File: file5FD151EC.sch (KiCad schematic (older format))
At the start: 5 parts, among them J3 Conn_ARM_JTAG_SWD_10

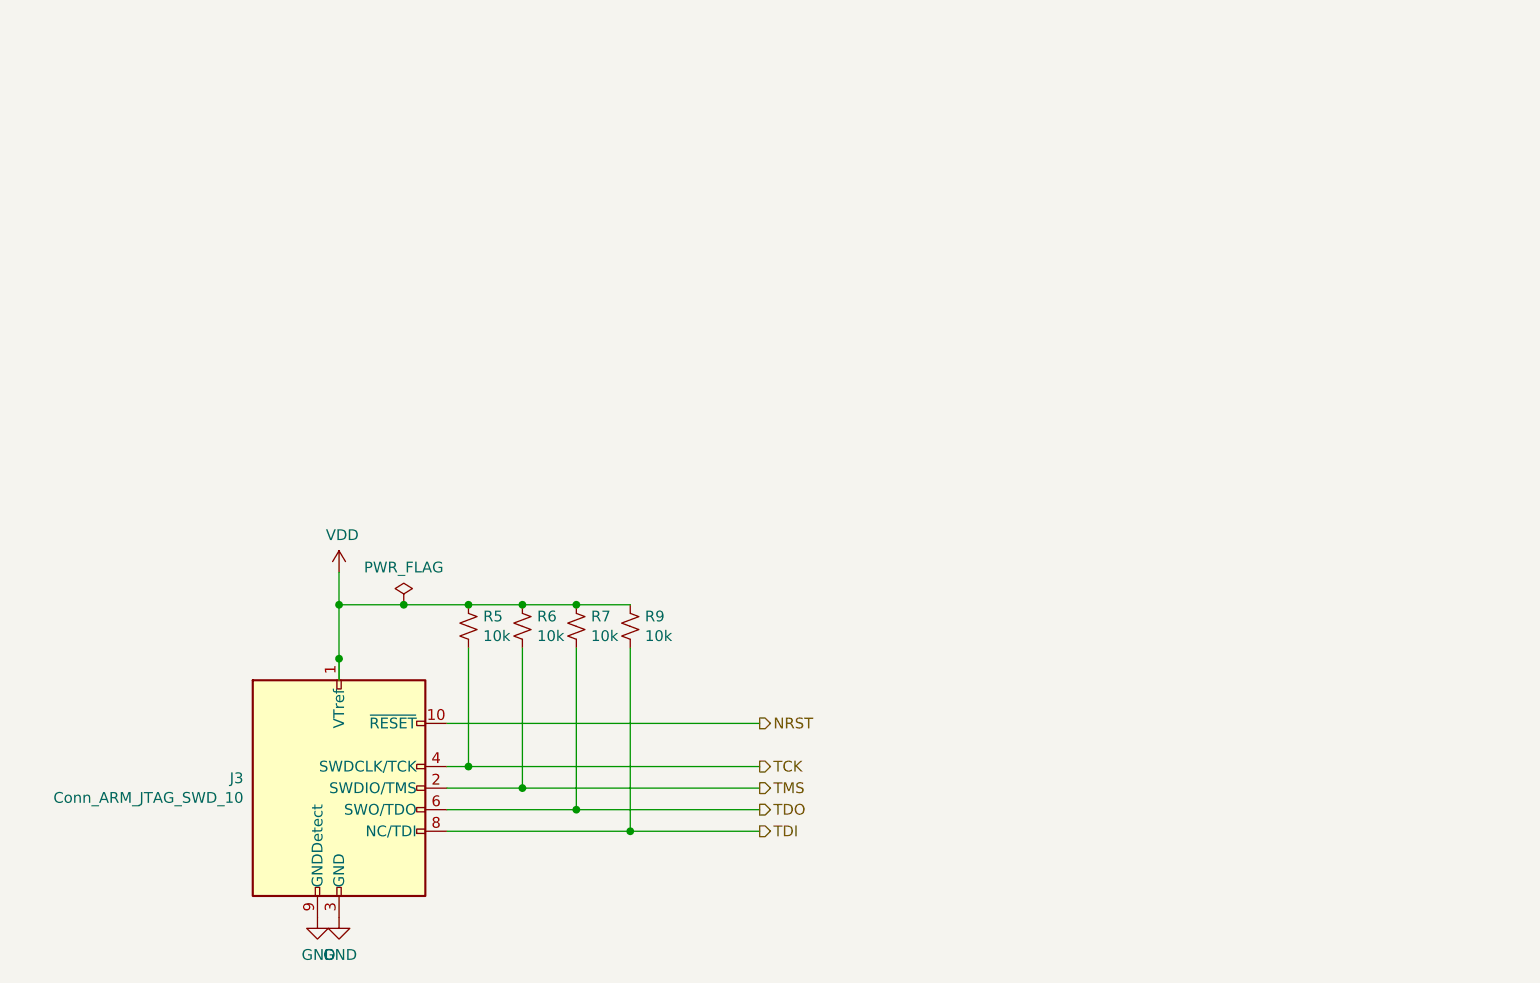
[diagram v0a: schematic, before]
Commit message: Change PS to SMPS 5v, LDO 3.3V
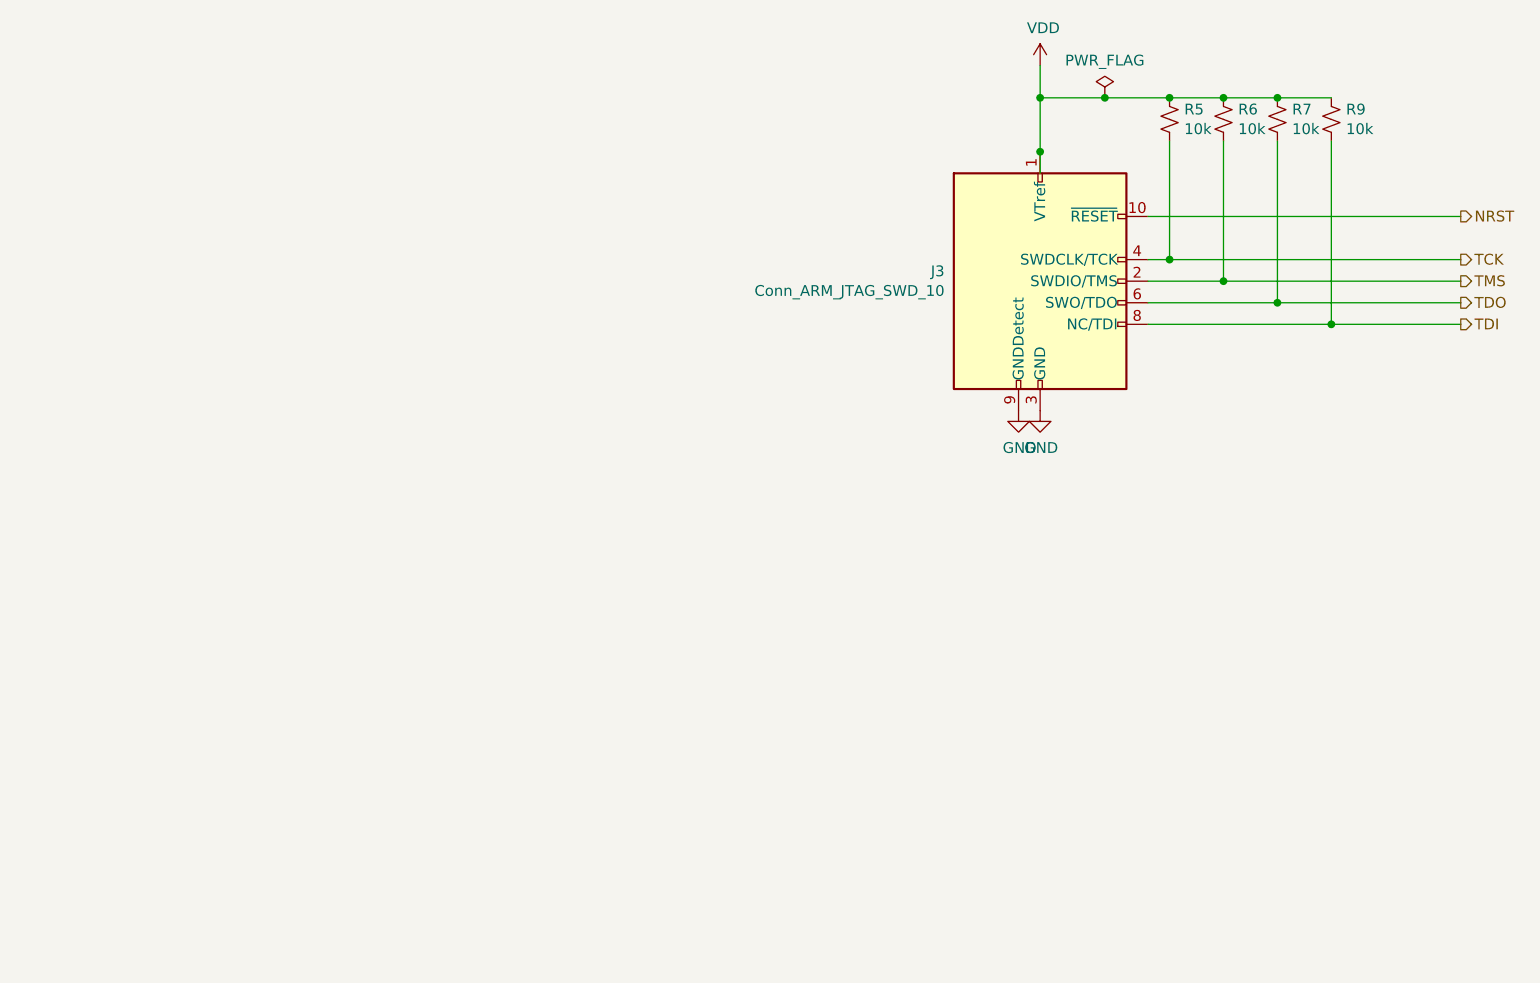
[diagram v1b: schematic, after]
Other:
- moved on the sheet: J3, R5, R6, R7, R9
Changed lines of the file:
@@
 $Descr A4 11693 8268
 encoding utf-8
-Sheet 4 5
+Sheet 4 6
 Title "KQ9P Power Controller 12VDC"
 Date "2020-12-08"
@@
 L Connector:Conn_ARM_JTAG_SWD_10 J3
 U 1 1 5FD1F74B
-P 2000 6500
-F 0 "J3" H 1557 6546 50  0000 R CNN
-F 1 "Conn_ARM_JTAG_SWD_10" H 1557 6455 50  0000 R CNN
-F 2 "" H 2000 6500 50  0001 C CNN
-F 3 "http://infocenter.arm.com/help/topic/com.arm.doc.ddi0314h/DDI0314H_coresight_components_trm.pdf" V 1650 5250 50  0001 C CNN
-	1    2000 6500
+P 5250 4150
+F 0 "J3" H 4807 4196 50  0000 R CNN
+F 1 "Conn_ARM_JTAG_SWD_10" H 4807 4105 50  0000 R CNN
+F 2 "" H 5250 4150 50  0001 C CNN
+F 3 "http://infocenter.arm.com/help/topic/com.arm.doc.ddi0314h/DDI0314H_coresight_components_trm.pdf" V 4900 2900 50  0001 C CNN
+	1    5250 4150
 	1    0    0    -1
 $EndComp
@@
 L power:GND #PWR03
 U 1 1 5FD1F751
-P 2000 7100
-F 0 "#PWR03" H 2000 6850 50  0001 C CNN
-F 1 "GND" H 2005 6927 50  0000 C CNN
-F 2 "" H 2000 7100 50  0001 C CNN
-F 3 "" H 2000 7100 50  0001 C CNN
-	1    2000 7100
+P 5250 4750
+F 0 "#PWR03" H 5250 4500 50  0001 C CNN
+F 1 "GND" H 5255 4577 50  0000 C CNN
+F 2 "" H 5250 4750 50  0001 C CNN
+F 3 "" H 5250 4750 50  0001 C CNN
+	1    5250 4750
 	1    0    0    -1
 $EndComp
@@
 L power:GND #PWR01
 U 1 1 5FD1F757
-P 1900 7100
-F 0 "#PWR01" H 1900 6850 50  0001 C CNN
-F 1 "GND" H 1905 6927 50  0000 C CNN
-F 2 "" H 1900 7100 50  0001 C CNN
-F 3 "" H 1900 7100 50  0001 C CNN
-	1    1900 7100
+P 5150 4750
+F 0 "#PWR01" H 5150 4500 50  0001 C CNN
+F 1 "GND" H 5155 4577 50  0000 C CNN
+F 2 "" H 5150 4750 50  0001 C CNN
+F 3 "" H 5150 4750 50  0001 C CNN
+	1    5150 4750
 	1    0    0    -1
 $EndComp
 Wire Wire Line
-	2500 6200 3950 6200
+	5750 3850 7200 3850
 Wire Wire Line
-	2500 6400 2600 6400
+	5750 4050 5850 4050
 Wire Wire Line
-	2500 6500 2850 6500
+	5750 4150 6100 4150
 Wire Wire Line
-	2500 6600 3100 6600
+	5750 4250 6350 4250
 Wire Wire Line
-	2500 6700 3350 6700
+	5750 4350 6600 4350
 $Comp
 L Device:R_Small_US R5
 U 1 1 5FD1F762
-P 2600 5750
-F 0 "R5" H 2668 5796 50  0000 L CNN
-F 1 "10k" H 2668 5705 50  0000 L CNN
-F 2 "" H 2600 5750 50  0001 C CNN
-F 3 "~" H 2600 5750 50  0001 C CNN
-	1    2600 5750
+P 5850 3400
+F 0 "R5" H 5918 3446 50  0000 L CNN
+F 1 "10k" H 5918 3355 50  0000 L CNN
+F 2 "" H 5850 3400 50  0001 C CNN
+F 3 "~" H 5850 3400 50  0001 C CNN
+	1    5850 3400
 	1    0    0    -1
 $EndComp
@@
 L Device:R_Small_US R6
 U 1 1 5FD1F768
-P 2850 5750
-F 0 "R6" H 2918 5796 50  0000 L CNN
-F 1 "10k" H 2918 5705 50  0000 L CNN
-F 2 "" H 2850 5750 50  0001 C CNN
-F 3 "~" H 2850 5750 50  0001 C CNN
-	1    2850 5750
+P 6100 3400
+F 0 "R6" H 6168 3446 50  0000 L CNN
+F 1 "10k" H 6168 3355 50  0000 L CNN
+F 2 "" H 6100 3400 50  0001 C CNN
+F 3 "~" H 6100 3400 50  0001 C CNN
+	1    6100 3400
 	1    0    0    -1
 $EndComp
@@
 L Device:R_Small_US R7
 U 1 1 5FD1F76E
-P 3100 5750
-F 0 "R7" H 3168 5796 50  0000 L CNN
-F 1 "10k" H 3168 5705 50  0000 L CNN
-F 2 "" H 3100 5750 50  0001 C CNN
-F 3 "~" H 3100 5750 50  0001 C CNN
-	1    3100 5750
+P 6350 3400
+F 0 "R7" H 6418 3446 50  0000 L CNN
+F 1 "10k" H 6418 3355 50  0000 L CNN
+F 2 "" H 6350 3400 50  0001 C CNN
+F 3 "~" H 6350 3400 50  0001 C CNN
+	1    6350 3400
 	1    0    0    -1
 $EndComp
@@
 L Device:R_Small_US R9
 U 1 1 5FD1F774
-P 3350 5750
-F 0 "R9" H 3418 5796 50  0000 L CNN
-F 1 "10k" H 3418 5705 50  0000 L CNN
-F 2 "" H 3350 5750 50  0001 C CNN
-F 3 "~" H 3350 5750 50  0001 C CNN
-	1    3350 5750
+P 6600 3400
+F 0 "R9" H 6668 3446 50  0000 L CNN
+F 1 "10k" H 6668 3355 50  0000 L CNN
+F 2 "" H 6600 3400 50  0001 C CNN
+F 3 "~" H 6600 3400 50  0001 C CNN
+	1    6600 3400
 	1    0    0    -1
 $EndComp
 Wire Wire Line
-	2000 5650 2300 5650
+	5250 3300 5550 3300
 Wire Wire Line
-	2000 5650 2000 5900
-Connection ~ 2000 5900
+	5250 3300 5250 3550
+Connection ~ 5250 3550
 Wire Wire Line
-	2000 5900 2000 6000
+	5250 3550 5250 3650
 Wire Wire Line
-	2600 5650 2850 5650
-Connection ~ 2600 5650
+	5850 3300 6100 3300
+Connection ~ 5850 3300
 Wire Wire Line
-	2850 5650 3100 5650
-Connection ~ 2850 5650
+	6100 3300 6350 3300
+Connection ~ 6100 3300
 Wire Wire Line
-	3100 5650 3350 5650
-Connection ~ 3100 5650
+	6350 3300 6600 3300
+Connection ~ 6350 3300
 Wire Wire Line
-	2600 5850 2600 6400
-Connection ~ 2600 6400
+	5850 3500 5850 4050
+Connection ~ 5850 4050
 Wire Wire Line
-	2600 6400 3950 6400
+	5850 4050 7200 4050
 Wire Wire Line
-	2850 5850 2850 6500
-Connection ~ 2850 6500
+	6100 3500 6100 4150
+Connection ~ 6100 4150
 Wire Wire Line
-	2850 6500 3950 6500
+	6100 4150 7200 4150
 Wire Wire Line
-	3100 5850 3100 6600
-Connection ~ 3100 6600
+	6350 3500 6350 4250
+Connection ~ 6350 4250
 Wire Wire Line
-	3100 6600 3950 6600
+	6350 4250 7200 4250
 Wire Wire Line
-	3350 5850 3350 6700
-Connection ~ 3350 6700
+	6600 3500 6600 4350
+Connection ~ 6600 4350
 Wire Wire Line
-	3350 6700 3950 6700
+	6600 4350 7200 4350
 $Comp
 L power:VDD #PWR02
 U 1 1 5FD1F795
-P 2000 5500
-F 0 "#PWR02" H 2000 5350 50  0001 C CNN
-F 1 "VDD" H 2015 5673 50  0000 C CNN
-F 2 "" H 2000 5500 50  0001 C CNN
-F 3 "" H 2000 5500 50  0001 C CNN
-	1    2000 5500
+P 5250 3150
+F 0 "#PWR02" H 5250 3000 50  0001 C CNN
+F 1 "VDD" H 5265 3323 50  0000 C CNN
+F 2 "" H 5250 3150 50  0001 C CNN
+F 3 "" H 5250 3150 50  0001 C CNN
+	1    5250 3150
 	1    0    0    -1
 $EndComp
 Wire Wire Line
-	2000 5500 2000 5650
-Connection ~ 2000 5650
+	5250 3150 5250 3300
+Connection ~ 5250 3300
 $Comp
 L power:PWR_FLAG #FLG0105
 U 1 1 5FD7E250
-P 2300 5650
-F 0 "#FLG0105" H 2300 5725 50  0001 C CNN
-F 1 "PWR_FLAG" H 2300 5823 50  0000 C CNN
-F 2 "" H 2300 5650 50  0001 C CNN
-F 3 "~" H 2300 5650 50  0001 C CNN
-	1    2300 5650
+P 5550 3300
+F 0 "#FLG0105" H 5550 3375 50  0001 C CNN
+F 1 "PWR_FLAG" H 5550 3473 50  0000 C CNN
+F 2 "" H 5550 3300 50  0001 C CNN
+F 3 "~" H 5550 3300 50  0001 C CNN
+	1    5550 3300
 	1    0    0    -1
 $EndComp
-Connection ~ 2300 5650
+Connection ~ 5550 3300
 Wire Wire Line
-	2300 5650 2600 5650
-Text HLabel 3950 6200 2    50   Output ~ 0
+	5550 3300 5850 3300
+Text HLabel 7200 3850 2    50   Output ~ 0
 NRST
-Text HLabel 3950 6400 2    50   Output ~ 0
+Text HLabel 7200 4050 2    50   Output ~ 0
 TCK
-Text HLabel 3950 6500 2    50   Output ~ 0
+Text HLabel 7200 4150 2    50   Output ~ 0
 TMS
-Text HLabel 3950 6600 2    50   Output ~ 0
+Text HLabel 7200 4250 2    50   Output ~ 0
 TDO
-Text HLabel 3950 6700 2    50   Output ~ 0
+Text HLabel 7200 4350 2    50   Output ~ 0
 TDI
 $EndSCHEMATC
